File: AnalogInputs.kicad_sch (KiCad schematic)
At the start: 45 parts

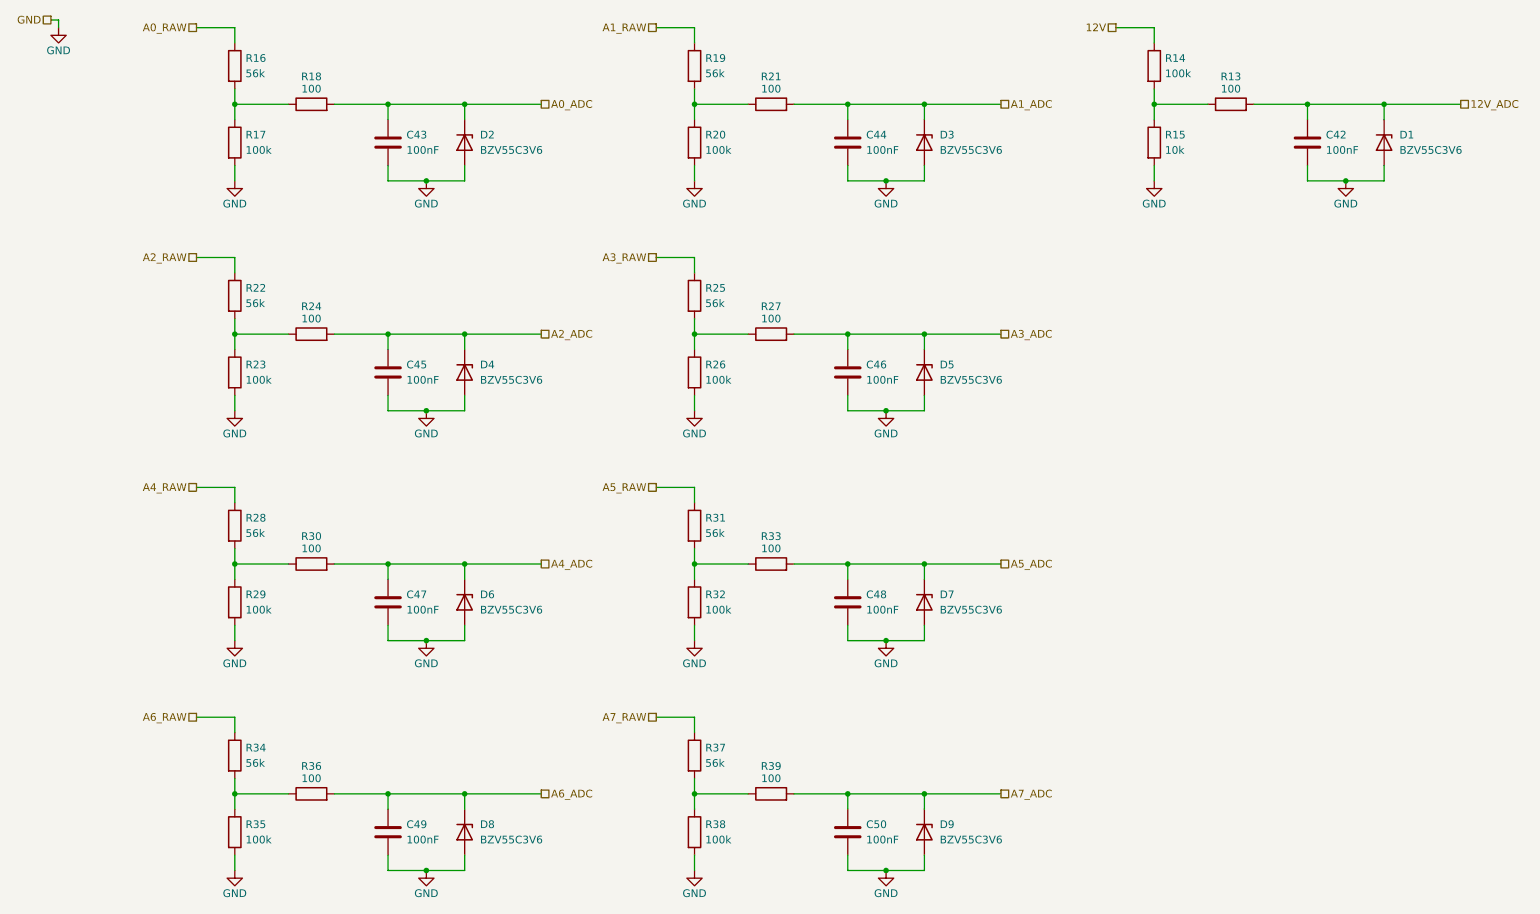
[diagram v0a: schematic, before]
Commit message: added lib to project and added molex superseal connector
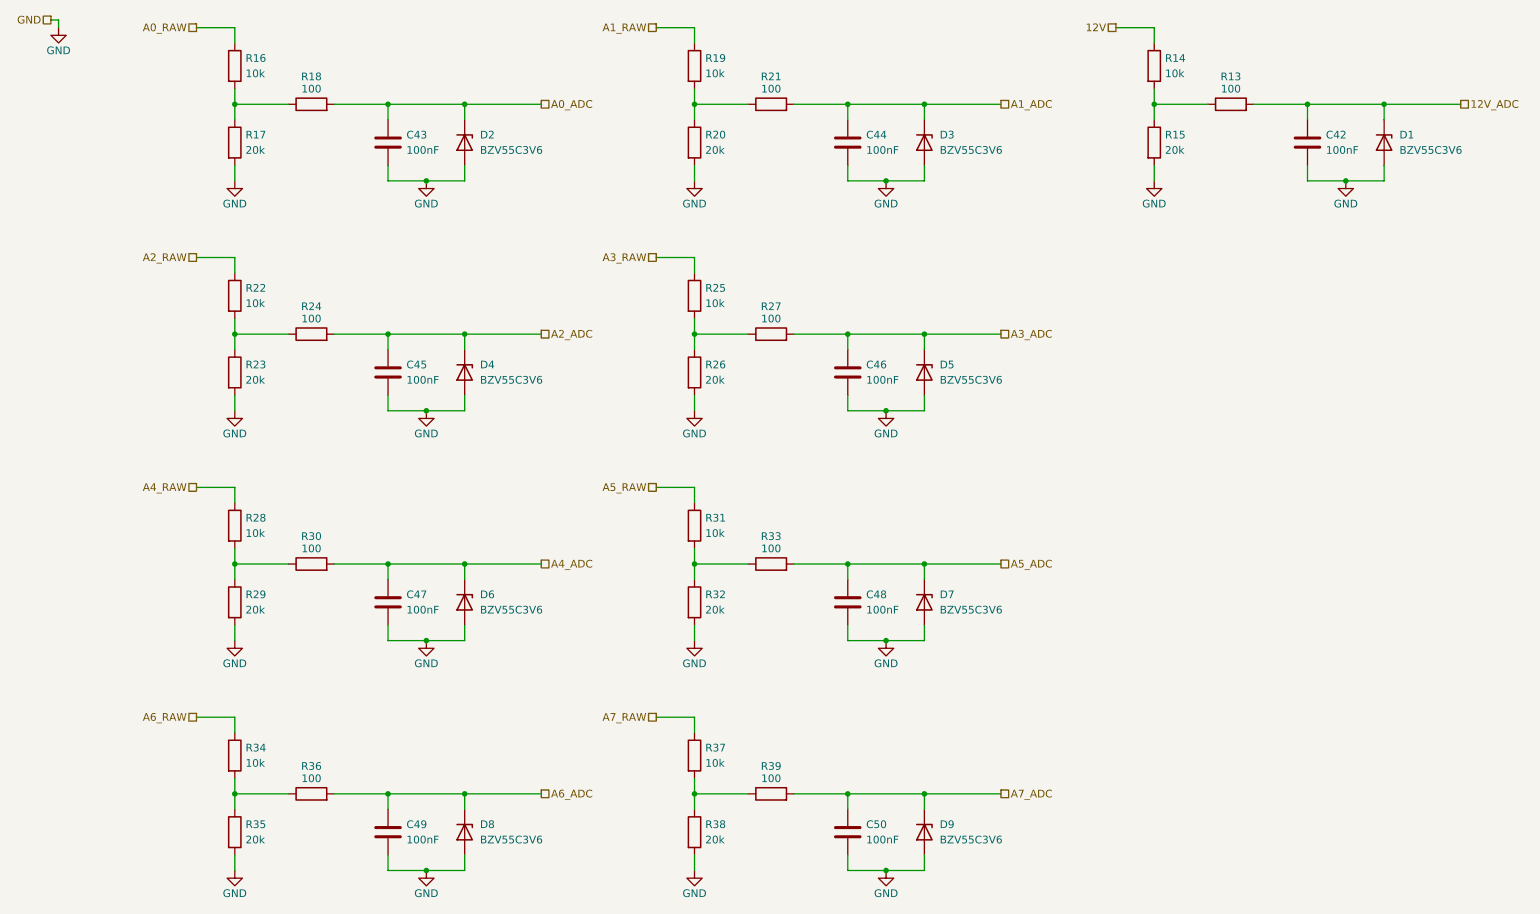
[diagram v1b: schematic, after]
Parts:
- R14: value 100k -> 10k
- R15: value 10k -> 20k
- R16, R19, R22, R25, R28, R31, R34, R37: value 56k -> 10k
- R17, R20, R23, R26, R29, R32, R35, R38: value 100k -> 20k
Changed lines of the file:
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@@
 			)
 		)
-		(property "Value" "56k"
+		(property "Value" "10k"
 			(at 128.778 140.97 0)
 			(effects
@@
 			)
 		)
-		(property "Value" "100k"
+		(property "Value" "20k"
 			(at 52.578 39.37 0)
 			(effects
@@
 			)
 		)
-		(property "Value" "56k"
+		(property "Value" "10k"
 			(at 52.578 102.87 0)
 			(effects
@@
 			)
 		)
-		(property "Value" "10k"
+		(property "Value" "20k"
 			(at 204.978 39.37 0)
 			(effects
@@
 			)
 		)
-		(property "Value" "56k"
+		(property "Value" "10k"
 			(at 52.578 26.67 0)
 			(effects
@@
 			)
 		)
-		(property "Value" "56k"
+		(property "Value" "10k"
 			(at 128.778 102.87 0)
 			(effects
@@
 			)
 		)
-		(property "Value" "56k"
+		(property "Value" "10k"
 			(at 52.578 64.77 0)
 			(effects
@@
 			)
 		)
-		(property "Value" "100k"
+		(property "Value" "20k"
 			(at 52.578 153.67 0)
 			(effects
@@
 			)
 		)
-		(property "Value" "100k"
+		(property "Value" "20k"
 			(at 52.578 77.47 0)
 			(effects
@@
 			)
 		)
-		(property "Value" "100k"
+		(property "Value" "20k"
 			(at 128.778 77.47 0)
 			(effects
@@
 			)
 		)
-		(property "Value" "100k"
+		(property "Value" "20k"
 			(at 128.778 115.57 0)
 			(effects
@@
 			)
 		)
-		(property "Value" "56k"
+		(property "Value" "10k"
 			(at 52.578 140.97 0)
 			(effects
@@
 			)
 		)
-		(property "Value" "100k"
+		(property "Value" "20k"
 			(at 128.778 39.37 0)
 			(effects
@@
 			)
 		)
-		(property "Value" "56k"
+		(property "Value" "10k"
 			(at 128.778 64.77 0)
 			(effects
@@
 			)
 		)
-		(property "Value" "100k"
+		(property "Value" "20k"
 			(at 128.778 153.67 0)
 			(effects
@@
 			)
 		)
-		(property "Value" "100k"
+		(property "Value" "10k"
 			(at 204.978 26.67 0)
 			(effects
@@
 			)
 		)
-		(property "Value" "100k"
+		(property "Value" "20k"
 			(at 52.578 115.57 0)
 			(effects
@@
 			)
 		)
-		(property "Value" "56k"
+		(property "Value" "10k"
 			(at 128.778 26.67 0)
 			(effects
